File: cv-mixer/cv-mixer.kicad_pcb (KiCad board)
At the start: 2 copper layers, 72.5 x 133.8 mm, 47 parts, among them J1 Input A1, J10 Pot, J11 Input B3, J12 Pot, J13 Pot, J14 Output A, J15 Pot, J16 Output B, J17 Power, J18 Power, J19 Power, J2 Pot, J3 Input A2, J4 Pot, J5 Input A3, J6 Pot, J7 Input B1, J8 Pot, J9 Input B2, U1 TL074

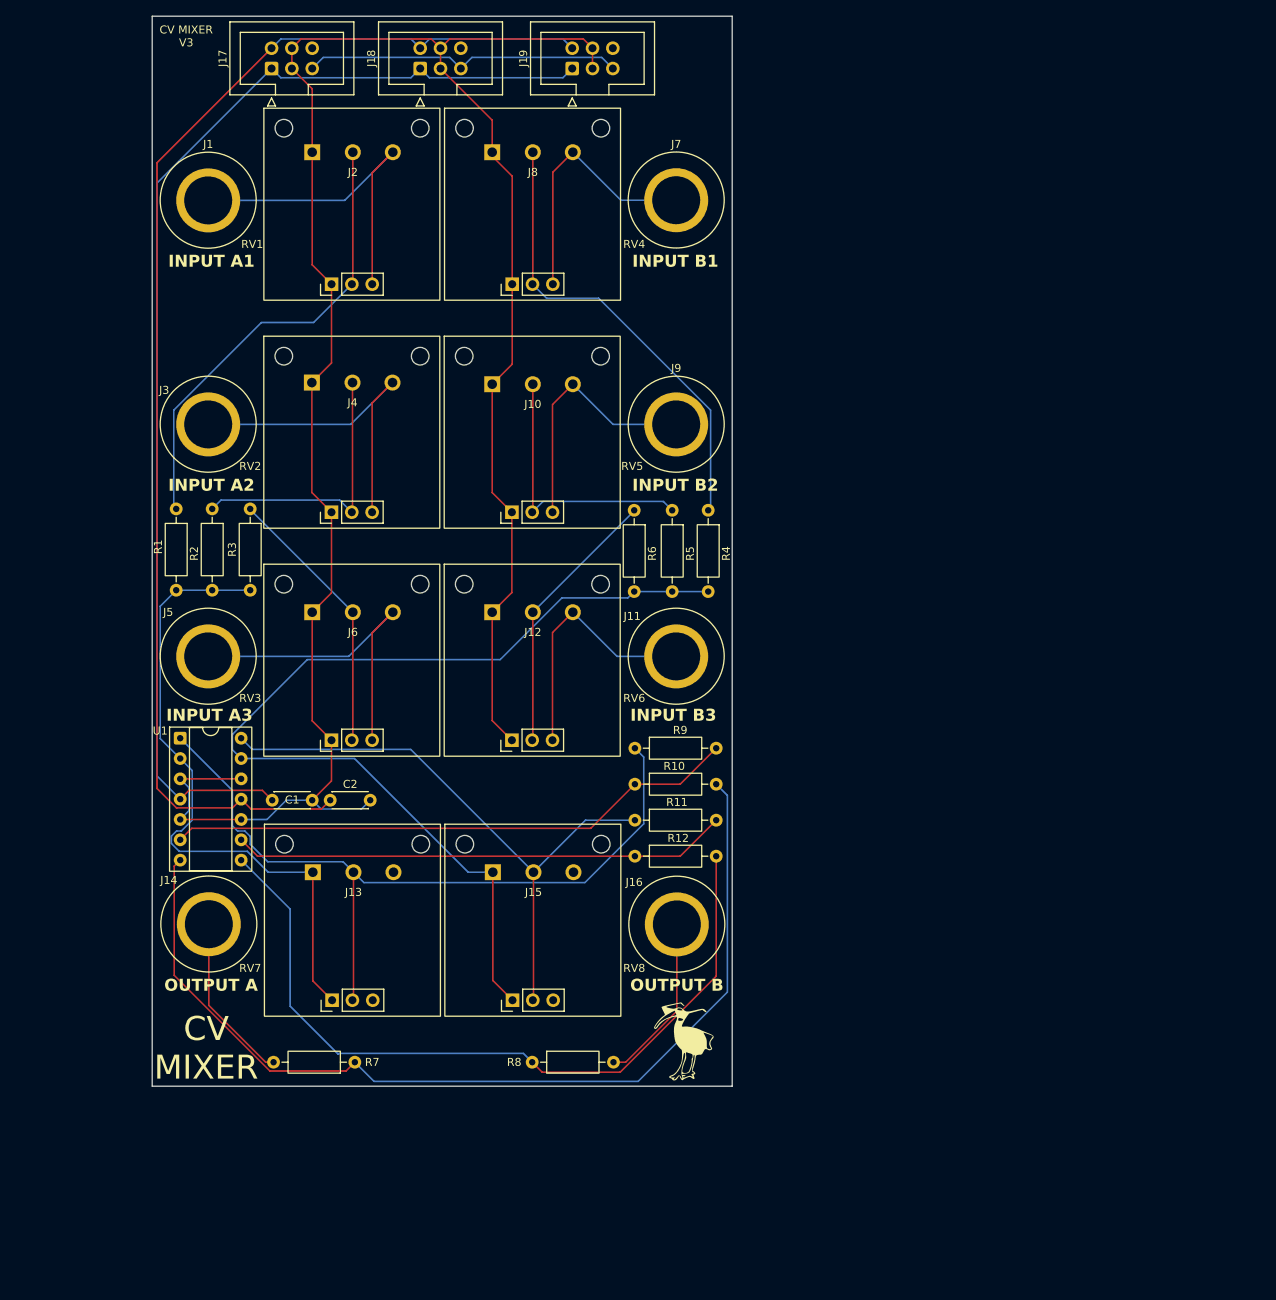
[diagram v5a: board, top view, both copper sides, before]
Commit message: Multilayer cv-mixer
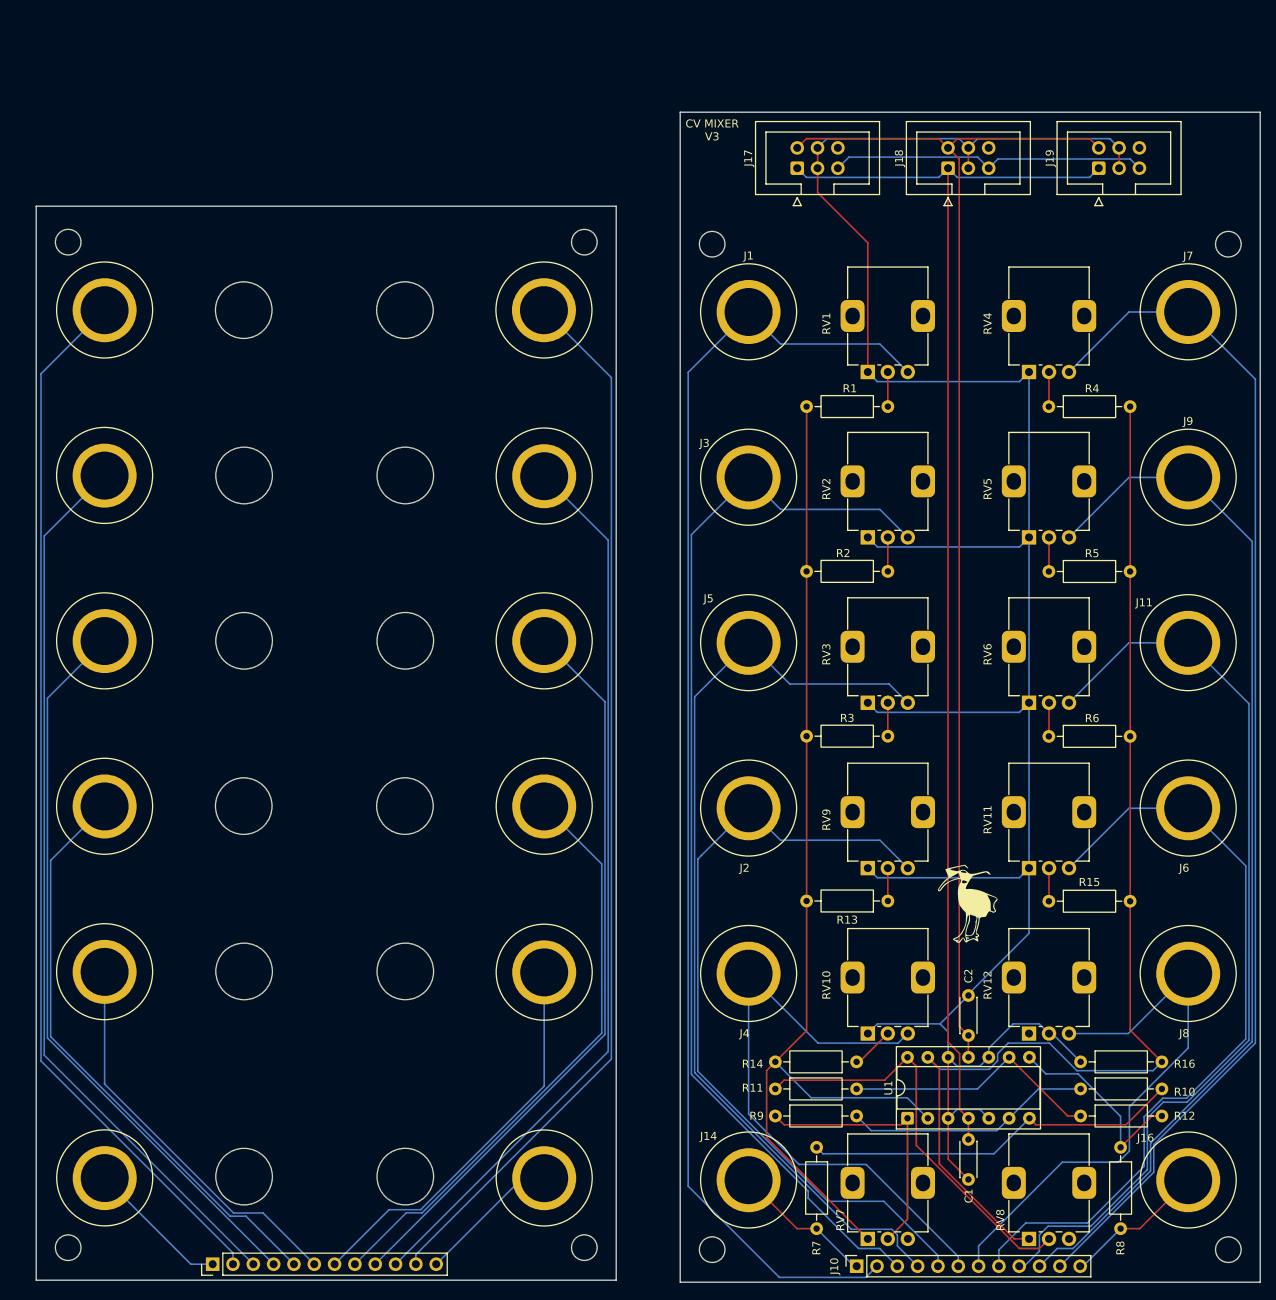
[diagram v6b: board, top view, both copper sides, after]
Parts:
- removed F1, F2, F3, F4: foot, modular2:foot
- added J20: Top A2, modular2:banana-jack, F.Cu at (25.1, 70.9)
- added J21: Top A3, modular2:banana-jack, F.Cu at (25.1, 91.6)
- added J22: Top A4, modular2:banana-jack, F.Cu at (25.1, 112.3)
- added J23: Top A5, modular2:banana-jack, F.Cu at (25.1, 132.9)
- added J24: Top B5, modular2:banana-jack, F.Cu at (80.0, 133.0)
- added J25: Top B4, modular2:banana-jack, F.Cu at (80.0, 112.3)
- added J26: Top B3, modular2:banana-jack, F.Cu at (80.0, 91.6)
- added J27: Top B2, modular2:banana-jack, F.Cu at (80.0, 71.0)
- added J28: Top B1, modular2:banana-jack, F.Cu at (80.0, 50.2)
- added J29: Top B, modular2:banana-jack, F.Cu at (80.0, 158.7)
- added R13: 100K, Resistor_THT:R_Axial_DIN0207_L6.3mm_D2.5mm_P10.16mm_Horizontal, F.Cu at (123.0, 124.1)
- added R14: 100K, Resistor_THT:R_Axial_DIN0207_L6.3mm_D2.5mm_P10.16mm_Horizontal, F.Cu at (119.1, 144.2)
- added R15: 100K, Resistor_THT:R_Axial_DIN0207_L6.3mm_D2.5mm_P10.16mm_Horizontal, F.Cu at (143.1, 124.1)
- added R16: 100K, Resistor_THT:R_Axial_DIN0207_L6.3mm_D2.5mm_P10.16mm_Horizontal, F.Cu at (147.1, 144.2)
- added REF**: MountingHole_3.2mm_M3, MountingHole:MountingHole_3.2mm_M3, F.Cu at (101.0, 167.7)
- added REF**: MountingHole_3.2mm_M3, MountingHole:MountingHole_3.2mm_M3, F.Cu at (20.5, 167.4)
- added REF**: MountingHole_3.2mm_M3, MountingHole:MountingHole_3.2mm_M3, F.Cu at (85.0, 41.7)
- added REF**: MountingHole_3.2mm_M3, MountingHole:MountingHole_3.2mm_M3, F.Cu at (20.5, 41.7)
- added REF**: MountingHole_3.2mm_M3, MountingHole:MountingHole_3.2mm_M3, F.Cu at (101.0, 42.0)
- added REF**: MountingHole_3.2mm_M3, MountingHole:MountingHole_3.2mm_M3, F.Cu at (85.0, 167.4)
- added REF**: MountingHole_3.2mm_M3, MountingHole:MountingHole_3.2mm_M3, F.Cu at (165.5, 167.7)
- added REF**: MountingHole_3.2mm_M3, MountingHole:MountingHole_3.2mm_M3, F.Cu at (165.5, 42.0)
- added RV10: 100K, modular2:Potentiometer_Alps_RK09K_Single_Vertical - knob padding, F.Cu at (120.5, 140.7)
- added RV11: 100K, modular2:Potentiometer_Alps_RK09K_Single_Vertical - knob padding, F.Cu at (140.6, 120.0)
- added RV12: 100K, modular2:Potentiometer_Alps_RK09K_Single_Vertical - knob padding, F.Cu at (140.6, 140.7)
- added RV9: 100K, modular2:Potentiometer_Alps_RK09K_Single_Vertical - knob padding, F.Cu at (120.5, 120.0)
- J10: value Pot -> Conn_01x12_Socket; footprint modular2:pot -> Connector_PinSocket_2.54mm:PinSocket_1x12_P2.54mm_Vertical
- J12: value Pot -> Conn_01x12_Pin; footprint modular2:pot -> Connector_PinHeader_2.54mm:PinHeader_1x12_P2.54mm_Vertical
- J13: value Pot -> Top A; footprint modular2:pot -> modular2:banana-jack
- J15: value Pot -> Top A1; footprint modular2:pot -> modular2:banana-jack
- J2: value Pot -> Input A4; footprint modular2:pot -> modular2:banana-jack
- J4: value Pot -> Input A5; footprint modular2:pot -> modular2:banana-jack
- J6: value Pot -> Input B4; footprint modular2:pot -> modular2:banana-jack
- J8: value Pot -> Input B5; footprint modular2:pot -> modular2:banana-jack
- RV1, RV2, RV3, RV4, RV5, RV6, RV7, RV8: footprint modular2:pot-socket -> modular2:Potentiometer_Alps_RK09K_Single_Vertical - knob padding
- moved J8 129.0 mm to (160.5, 133.2)
- moved J10 114.6 mm to (119.1, 169.8), turned to 90 degrees
- moved J6 106.6 mm to (160.5, 112.5)
- moved U1 102.6 mm to (125.4, 151.3), turned to 90 degrees
- moved C1 94.7 mm to (133.0, 158.9), turned to 90 degrees
- moved J2 93.2 mm to (105.6, 112.5)
- moved J15 90.8 mm to (25.1, 50.2)
- moved R1 89.9 mm to (123.0, 62.3), turned to 180 degrees
- moved J12 88.1 mm to (38.6, 169.5), turned to 90 degrees
- moved J4 86.4 mm to (105.6, 133.2)
- moved R2 84.8 mm to (123.0, 82.9), turned to 180 degrees
- moved R3 84.6 mm to (123.0, 103.5), turned to 180 degrees
- moved C2 78.7 mm to (133.0, 135.9), turned to -90 degrees
- moved RV7 75.6 mm to (120.5, 166.3), turned to 90 degrees
- moved J14 74.7 mm to (105.6, 159.0)
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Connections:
- J10 pad 1: GND -> Net-(J10-Pin_1)
- J10 pad 2: Net-(J10-Pin_2) -> Net-(J1-Pin_1)
- J11 pad 1: Net-(J11-Pin_1) -> Net-(J10-Pin_9)
- J12 pad 1: GND -> Net-(J12-Pin_1)
- J12 pad 3: Net-(J11-Pin_1) -> Net-(J12-Pin_3)
- J13 pad 1: Net-(J13-Pin_1) -> Net-(J12-Pin_1)
- J14 pad 1: Net-(J14-Pin_1) -> Net-(J10-Pin_1)
- J15 pad 1: Net-(J15-Pin_1) -> Net-(J12-Pin_2)
- J16 pad 1: Net-(J16-Pin_1) -> Net-(J10-Pin_12)
- J2 pad 1: GND -> Net-(J10-Pin_5)
- J3 pad 1: Net-(J3-Pin_1) -> Net-(J10-Pin_3)
- J4 pad 1: GND -> Net-(J10-Pin_6)
- J5 pad 1: Net-(J5-Pin_1) -> Net-(J10-Pin_4)
- J6 pad 1: GND -> Net-(J10-Pin_8)
- J7 pad 1: Net-(J7-Pin_1) -> Net-(J10-Pin_11)
- J8 pad 1: GND -> Net-(J10-Pin_7)
- J9 pad 1: Net-(J10-Pin_3) -> Net-(J10-Pin_10)
- R1 pad 1: Net-(J2-Pin_2) -> Net-(R1-Pad1)
- R1 pad 2: Net-(J13-Pin_1) -> Net-(U1A--)
- R11 pad 1: Net-(J15-Pin_2) -> Net-(R11-Pad1)
- R2 pad 1: Net-(J4-Pin_2) -> Net-(R2-Pad1)
- R2 pad 2: Net-(J13-Pin_1) -> Net-(U1A--)
- R3 pad 1: Net-(J6-Pin_2) -> Net-(R3-Pad1)
- R3 pad 2: Net-(J13-Pin_1) -> Net-(U1A--)
- R4 pad 1: Net-(J8-Pin_2) -> Net-(R4-Pad1)
- R4 pad 2: Net-(J15-Pin_1) -> Net-(U1D--)
- R5 pad 1: Net-(J10-Pin_2) -> Net-(R5-Pad1)
- R5 pad 2: Net-(J15-Pin_1) -> Net-(U1D--)
- R6 pad 1: Net-(J12-Pin_2) -> Net-(R6-Pad1)
- R6 pad 2: Net-(J15-Pin_1) -> Net-(U1D--)
- R7 pad 2: Net-(J14-Pin_1) -> Net-(J10-Pin_1)
- R8 pad 2: Net-(J16-Pin_1) -> Net-(J10-Pin_12)
- R9 pad 1: Net-(J13-Pin_2) -> Net-(R9-Pad1)
- RV1 pad 2: Net-(J2-Pin_2) -> Net-(R1-Pad1)
- RV2 pad 2: Net-(J4-Pin_2) -> Net-(R2-Pad1)
- RV2 pad 3: Net-(J3-Pin_1) -> Net-(J10-Pin_3)
- RV3 pad 2: Net-(J6-Pin_2) -> Net-(R3-Pad1)
- RV3 pad 3: Net-(J5-Pin_1) -> Net-(J10-Pin_4)
- RV4 pad 2: Net-(J8-Pin_2) -> Net-(R4-Pad1)
- RV4 pad 3: Net-(J7-Pin_1) -> Net-(J10-Pin_11)
- RV5 pad 2: Net-(J10-Pin_2) -> Net-(R5-Pad1)
- RV5 pad 3: Net-(J10-Pin_3) -> Net-(J10-Pin_10)
- RV6 pad 2: Net-(J12-Pin_2) -> Net-(R6-Pad1)
- RV6 pad 3: Net-(J11-Pin_1) -> Net-(J10-Pin_9)
- RV7 pad 1: Net-(J13-Pin_1) -> Net-(U1A--)
- RV7 pad 2: Net-(J13-Pin_2) -> Net-(R9-Pad1)
- RV8 pad 1: Net-(J15-Pin_1) -> Net-(U1D--)
- RV8 pad 2: Net-(J15-Pin_2) -> Net-(R11-Pad1)
- U1 pad 1: Net-(J13-Pin_2) -> Net-(R9-Pad1)
- U1 pad 13: Net-(J15-Pin_1) -> Net-(U1D--)
- U1 pad 14: Net-(J15-Pin_2) -> Net-(R11-Pad1)
- U1 pad 2: Net-(J13-Pin_1) -> Net-(U1A--)
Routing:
- net Net-(J10-Pin_11): track 0.00 -> 150.9 mm
- net Net-(U1D--): track 0.00 -> 146.2 mm
- net Net-(U1A--): track 0.00 -> 133.3 mm
- net Net-(J12-Pin_11): track 0.00 -> 132.9 mm
- net Net-(J10-Pin_10): track 0.00 -> 132.1 mm
- net Net-(J15-Pin_1): track 124.7 -> 0.00 mm
- net Net-(J1-Pin_1): track 43.1 -> 164.3 mm
- net Net-(J10-Pin_4): track 0.00 -> 118.2 mm
- net Net-(J10-Pin_9): track 0.00 -> 116.2 mm
- net Net-(J12-Pin_10): track 0.00 -> 112.8 mm
- net Net-(J12-Pin_3): track 0.00 -> 112.5 mm
- net Net-(J10-Pin_3): track 32.1 -> 136.8 mm
- net Net-(J10-Pin_5): track 0.00 -> 99.4 mm
- net Net-(J12-Pin_2): track 34.0 -> 132.5 mm
- net Net-(J13-Pin_2): track 97.6 -> 0.00 mm
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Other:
- board size 72.5 x 133.8 mm -> 153 x 146.2 mm
- board text removed: "CV MIXER"
- board text removed: "INPUT A1"
- board text removed: "INPUT A2"
- board text removed: "INPUT A3"
- board text removed: "INPUT B1"
- board text removed: "INPUT B2"
- board text removed: "INPUT B3"
- board text removed: "OUTPUT A"
- board text removed: "OUTPUT B"

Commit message: Update some designs
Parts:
- added REF**: MountingHole_3.2mm_M3, MountingHole:MountingHole_3.2mm_M3, F.Cu at (160.5, 102.1)
- added REF**: MountingHole_3.2mm_M3, MountingHole:MountingHole_3.2mm_M3, F.Cu at (22.6, 102.4)
- added REF**: MountingHole_3.2mm_M3, MountingHole:MountingHole_3.2mm_M3, F.Cu at (77.5, 102.4)
- added REF**: MountingHole_3.2mm_M3, MountingHole:MountingHole_3.2mm_M3, F.Cu at (105.6, 102.1)
- moved J12 2.55 mm to (36.1, 170.0)
- moved J13 2.55 mm to (22.6, 159.2)
- moved J15 2.55 mm to (22.6, 50.7)
- moved J20 2.55 mm to (22.6, 71.4)
- moved J21 2.55 mm to (22.6, 92.1)
- moved J22 2.55 mm to (22.6, 112.8)
- moved J23 2.55 mm to (22.6, 133.4)
- moved J24 2.55 mm to (77.5, 133.5)
- moved J25 2.55 mm to (77.5, 112.8)
- moved J26 2.55 mm to (77.5, 92.1)
- moved J27 2.55 mm to (77.5, 71.5)
- moved J28 2.55 mm to (77.5, 50.7)
- moved J29 2.55 mm to (77.5, 159.2)
- moved REF** 2.55 mm to (82.5, 167.9)
- moved REF** 2.55 mm to (18.0, 167.9)
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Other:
- board size 153 x 146.2 mm -> 155.5 x 146.5 mm
